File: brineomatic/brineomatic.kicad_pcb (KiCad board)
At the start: 2 copper layers, 117 parts, among them J1 SENSOR, J10 Solenoid, J11 Solenoid, J12 SENSOR, J13 SERVO, J14 TDS, J15 POWER, J2 Conn_01x03, J3 Conn_01x03, J4 THERMISTOR, J5 SERVO, J6 Solenoid, J7 MOTOR, J8 Solenoid, J9 Solenoid, Q1 AO3400A, Q2 AON7524, Q3 AO3400A, Q4 AO3400A, Q5 AO3400A, U1 ESP32-S3-DEVKITC, U2 XL1509-5.0, U3 ADS1115IDGS, U4 DRV8871DDA, U5 XL1509-5.0, U6 XL1509-5.0

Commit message: starting to look good.
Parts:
- removed C18: 100nF, Capacitor_SMD:C_0805_2012Metric_Pad1.18x1.45mm_HandSolder
- removed C19: 10uF/35v, Capacitor_SMD:C_1206_3216Metric_Pad1.33x1.80mm_HandSolder
- removed C20: 100uF / 10v, Capacitor_Tantalum_SMD:CP_EIA-3528-21_Kemet-B
- removed D10: LED, LED_SMD:LED_0805_2012Metric_Pad1.15x1.40mm_HandSolder
- removed D11: SS54, Diode_SMD:D_SMA
- removed D19: DSK24, Diode_SMD:D_SOD-123
- removed F4: mSMD150, Fuse:Fuse_1812_4532Metric_Pad1.30x3.40mm_HandSolder
- removed J13, J5: SERVO, Connector_PinHeader_2.54mm:PinHeader_1x03_P2.54mm_Vertical
- removed JP1, JP2: For Testing, Jumper:SolderJumper-2_P1.3mm_Open_RoundedPad1.0x1.5mm
- removed L4: SMMS0650-680M, Inductor_SMD:L_Chilisin_BMRB00060650
- removed Q2: AON7524, Package_DFN_QFN:DFN-8-1EP_3x3mm_P0.5mm_EP1.7x2.4mm
- removed R19, R20: 1k, Resistor_SMD:R_0805_2012Metric_Pad1.20x1.40mm_HandSolder
- removed R2, R32: 10.2K 0.1%, Resistor_SMD:R_1206_3216Metric_Pad1.30x1.75mm_HandSolder
- removed R21: 100k, Resistor_SMD:R_0805_2012Metric_Pad1.20x1.40mm_HandSolder
- removed R3, R33: 19.8K 0.1%, Resistor_SMD:R_1206_3216Metric_Pad1.30x1.75mm_HandSolder
- removed U6: XL1509-5.0, Package_SO:SOIC-8_3.9x4.9mm_P1.27mm
- C10: value 22uF / 63v -> 22uF / 50v; footprint Capacitor_SMD:CP_Elec_6.3x7.7 -> Capacitor_SMD:CP_Elec_6.3x5.4
- D3: value DSK24 -> DSK34
- J1, J12: value SENSOR -> PRESSURE; footprint TerminalBlock_Phoenix:TerminalBlock_Phoenix_PT-1,5-2-3.5-H_1x02_P3.50mm_Horizontal -> Connector_JST:JST_PH_S2B-PH-K_1x02_P2.00mm_Horizontal
- J10, J11, J6, J7, J9: footprint Connector_Phoenix_MSTB:PhoenixContact_MSTBA_2,5_2-G-5,08_1x02_P5.08mm_Horizontal -> Connector_Phoenix_MC:PhoenixContact_MC_1,5_2-G-3.5_1x02_P3.50mm_Horizontal
- J14: footprint TerminalBlock_Phoenix:TerminalBlock_Phoenix_PT-1,5-3-3.5-H_1x03_P3.50mm_Horizontal -> Connector_JST:JST_PH_S3B-PH-K_1x03_P2.00mm_Horizontal
- J15: footprint Connector_Phoenix_MSTB:PhoenixContact_MSTBA_2,5_2-G-5,08_1x02_P5.08mm_Horizontal -> Connector_Phoenix_MC_HighVoltage:PhoenixContact_MC_1,5_2-G-5.08_1x02_P5.08mm_Horizontal
- J2: value Conn_01x03 -> FLOWMETER; footprint TerminalBlock_Phoenix:TerminalBlock_Phoenix_PT-1,5-3-3.5-H_1x03_P3.50mm_Horizontal -> Connector_JST:JST_PH_S3B-PH-K_1x03_P2.00mm_Horizontal
- J3: value Conn_01x03 -> DS18B20; footprint TerminalBlock_Phoenix:TerminalBlock_Phoenix_PT-1,5-3-3.5-H_1x03_P3.50mm_Horizontal -> Connector_JST:JST_PH_S3B-PH-K_1x03_P2.00mm_Horizontal
- J4: footprint TerminalBlock_Phoenix:TerminalBlock_Phoenix_PT-1,5-2-3.5-H_1x02_P3.50mm_Horizontal -> Connector_JST:JST_PH_S2B-PH-K_1x02_P2.00mm_Horizontal
- J8: value Solenoid -> SERVOS; footprint Connector_Phoenix_MSTB:PhoenixContact_MSTBA_2,5_2-G-5,08_1x02_P5.08mm_Horizontal -> Connector_PinHeader_2.54mm:PinHeader_2x03_P2.54mm_Horizontal
- L1: value SMMS0650-680M -> 2.5A 68uH; footprint Inductor_SMD:L_Chilisin_BMRB00060650 -> Inductor_SMD:L_Sunlord_MWSA1003S
- R9: footprint Resistor_SMD:R_1206_3216Metric_Pad1.30x1.75mm_HandSolder -> Resistor_SMD:R_0805_2012Metric_Pad1.20x1.40mm_HandSolder
- U1: footprint yarrboard:Waveshare-ESP32-S3-dev-kit -> yarrboard:Waveshare-ESP32-S3-dev-kit-SMD
- moved H2 164.1 mm to (66.3, 89.2), turned to 180 degrees
- moved R10 161.5 mm to (69.2, 41.2)
- moved C3 161.3 mm to (69.2, 39.0)
- moved J4 157.6 mm to (65.5, 38.0), turned to -90 degrees
- moved R35 157.2 mm to (69.5, 57.5)
- moved R9 156.8 mm to (69.2, 36.8), turned to 180 degrees
- moved C21 152.2 mm to (69.5, 59.8), turned to 180 degrees
- moved J14 151.6 mm to (65.5, 55.0), turned to -90 degrees
- moved D20 148.1 mm to (69.5, 54.5)
- moved J1 140.7 mm to (65.5, 81.5), turned to -90 degrees
- moved J3 139.4 mm to (65.5, 45.5), turned to -90 degrees
- moved R8 138.0 mm to (68.5, 46.5), turned to 90 degrees
- moved D1 135.9 mm to (69.5, 84.2)
- moved C1 129.7 mm to (69.5, 79.5), turned to 180 degrees
- moved R4 129.6 mm to (69.5, 81.5)
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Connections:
- C1 pad 1: /ADC/ADC0 -> /ADC/ADC3
- C17 pad 1: /ADC/ADC1 -> /ADC/ADC2
- C21 pad 1: /ADC/ADC2 -> /ADC/ADC1
- C3 pad 1: /ADC/ADC3 -> /ADC/ADC0
- C6 pad 1: Net-(J5-Pin_2) -> Net-(U2-FB)
- F1 pad 1: Net-(J5-Pin_2) -> Net-(J8-Pin_3)
- J1 pad 2: Net-(J1-Pin_2) -> Net-(D1-COM)
- J12 pad 2: Net-(J12-Pin_2) -> Net-(D18-COM)
- J8 pad 1: +24V -> /Servo 1/SERVO1
- J8 pad 2: Net-(D11-A) -> /Servo 1/SERVO2
- R1 pad 2: Net-(J1-Pin_2) -> Net-(D1-COM)
- R10 pad 2: /ADC/ADC3 -> /ADC/ADC0
- R31 pad 2: Net-(J12-Pin_2) -> Net-(D18-COM)
- R34 pad 2: /ADC/ADC1 -> /ADC/ADC2
- R35 pad 2: /ADC/ADC2 -> /ADC/ADC1
- R4 pad 2: /ADC/ADC0 -> /ADC/ADC3
- U1 pad 17: unconnected-(U1-GPIO11-Pad17) -> /Flowmeter/OUTPUT
- U1 pad 27: unconnected-(U1-GPIO21-Pad27) -> /Solenoid Driver 1/INPUT
- U1 pad 28: unconnected-(U1-GPIO47-Pad28) -> /Solenoid Driver 2/INPUT
- U1 pad 29: unconnected-(U1-GPIO48-Pad29) -> /Solenoid Driver 3/INPUT
- U1 pad 33: unconnected-(U1-GPIO36-Pad33) -> /Solenoid Driver 4/INPUT
- U1 pad 36: unconnected-(U1-GPIO39-Pad36) -> /Servo 1/SERVO1
- U1 pad 37: unconnected-(U1-GPIO40-Pad37) -> /Servo 1/SERVO2
- U1 pad 38: unconnected-(U1-GPIO41-Pad38) -> /DC Motor Driver/IN1
- U1 pad 39: unconnected-(U1-GPIO42-Pad39) -> /DC Motor Driver/IN2
- U1 pad 6: unconnected-(U1-GPIO6-Pad6) -> /Temperature - DS18B20/OUTPUT
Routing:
- net +24V: track 0.00 -> 286.0 mm
- net +3.3V: track 0.00 -> 107.3 mm
- net +5V: track 0.00 -> 106.1 mm
- net ESP32_5V: track 0.00 -> 89.7 mm
- net /Solenoid Driver 4/INPUT: track 0.00 -> 42.1 mm
- net /ADC/ADC3: track 0.00 -> 39.7 mm, vias 0 -> 2
- net /Servo 1/SERVO2: track 0.00 -> 38.1 mm
- net Net-(U2-FB): track 0.00 -> 35.8 mm
- net /Servo 1/SERVO1: track 0.00 -> 35.5 mm
- net /ADC/ADC2: track 0.00 -> 31.2 mm, vias 0 -> 2
- net /Solenoid Driver 3/INPUT: track 0.00 -> 29.5 mm
- net SCL: track 0.00 -> 25.7 mm
- net Net-(D3-K): track 0.00 -> 20.6 mm
- net Net-(D8-K): track 0.00 -> 20.5 mm
- net /Solenoid Driver 2/INPUT: track 0.00 -> 20.3 mm
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- added copper zone on B.Cu, net GND
- added copper zone on F.Cu, net GND
- added copper zone on In1.Cu, net GND
- added copper zone on In2.Cu, net GND
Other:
- board outline added: 90 x 63.5 mm
- copper layers 2 -> 4
- board text added: "DC MOTOR + -"
- board text added: "S + -"
- board text added: "SERVOS"
- board text added: "SOLENOID 1"
- board text added: "SOLENOID 2"
- board text added: "SOLENOID 3"
- board text added: "SOLENOID 4"

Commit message: silkscreen and more layout tweaks.
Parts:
- added SYM1: Logo_Open_Hardware_Small, Symbol:OSHW-Logo_11.4x12mm_SilkScreen, F.Cu at (113.5, 61.2)
- added SYM2: Logo_Open_Hardware_Small, yarrboard:Logo Small, F.Cu at (91.5, 48.2)
- moved C9 1.08 mm to (117.4, 39.5), turned to 90 degrees
- moved C12 0.45 mm to (140.2, 50.7)
- moved C13 0.45 mm to (144.5, 50.7)
- moved C15 0.40 mm to (148.2, 51.3)
- moved D6 0.40 mm to (137.0, 41.9)
- moved C14 0.30 mm to (144.5, 52.7)
- moved R18 0.30 mm to (140.3, 52.7)
- moved D7 0.25 mm to (138.5, 47.5)
- moved C2 0.20 mm to (69.5, 69.3)
- moved L2 0.15 mm to (144.5, 47.1)
- moved J15 0.08 mm to (143.0, 33.1)
- moved J7 0.08 mm to (113.7, 33.1)
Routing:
- net +24V: track 286.0 -> 292.1 mm
- net /Flowmeter/OUTPUT: track 17.9 -> 19.1 mm
- net ESP32_5V: track 89.7 -> 90.4 mm
- net GND: vias 123 -> 139
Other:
- board text added: "-POWER+"
- board text added: "BRINEOMATIC"
- board text added: "FLOW LOPRES HIPRES"
- board text added: "REV A"
- board text added: "THERM DS18B20 TDS"
- board text added: "github.com/hoeken/brineomatic"

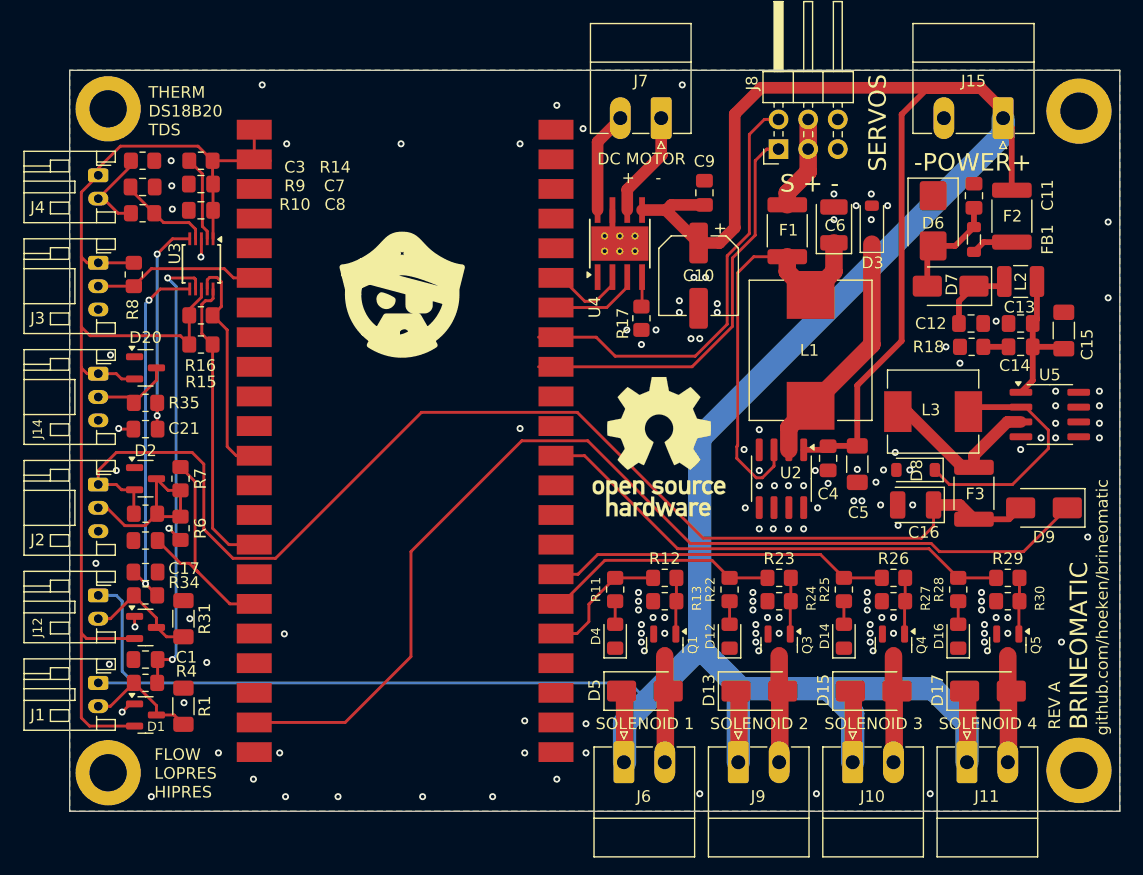
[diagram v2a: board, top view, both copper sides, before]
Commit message: updated bom and prepping for Rev A
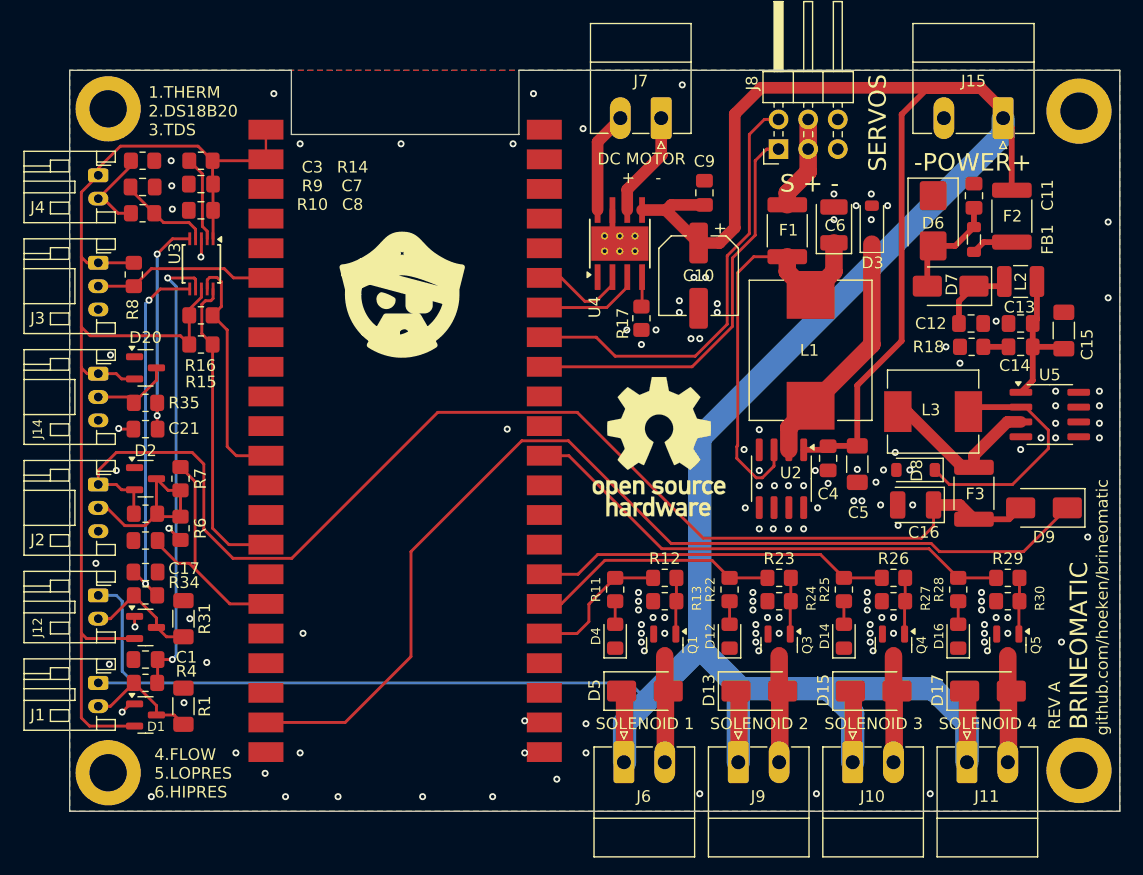
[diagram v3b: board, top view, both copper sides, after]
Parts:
- D7, D9: value SS34 -> SS54
- J1, J12: value PRESSURE -> ~
- J10, J11, J6, J9: value Solenoid -> 3.5MM
- J14: value TDS -> ~
- J15: value POWER -> 5.08MM
- J2: value FLOWMETER -> ~
- J3: value DS18B20 -> ~
- J4: value THERMISTOR -> ~
- J7: value MOTOR -> 3.5MM
- R14: value 10k -> 10K
- R17: value 30k -> 30K
- R7: value 5k -> 4.7K
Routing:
- net /Flowmeter/OUTPUT: track 19.1 -> 20.9 mm
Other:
- outline, holes or cut-outs redrawn
- board text added: "1.THERM 2.DS18B20 3.TDS"
- board text added: "4.FLOW 5.LOPRES 6.HIPRES"
- board text removed: "FLOW LOPRES HIPRES"
- board text removed: "THERM DS18B20 TDS"

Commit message: updates parts, footprints, etc.  ready for production.
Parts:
- J15: footprint Connector_Phoenix_MC_HighVoltage:PhoenixContact_MC_1,5_2-G-5.08_1x02_P5.08mm_Horizontal -> Connector_Phoenix_MSTB:PhoenixContact_MSTBA_2,5_2-G-5,08_1x02_P5.08mm_Horizontal
- R12, R23, R26, R29: value 1k -> 100R
- U3: value ADS1115IDGS -> ADS1115IDGSR
- moved J15 2.15 mm to (142.3, 35.1)
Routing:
- net Net-(U2-FB): track 35.8 -> 32.0 mm
- net +24V: track 292.1 -> 289.8 mm
- net /Servo 1/SERVO1: track 35.5 -> 36.6 mm
- net /Servo 1/SERVO2: track 38.1 -> 39.2 mm
- net GND: vias 139 -> 138
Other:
- board text added: "POWER - +"
- board text removed: "-POWER+"

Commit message: worked on schematic and layout a bit more.
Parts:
- removed C10: 22uF / 50v, Capacitor_SMD:CP_Elec_6.3x5.4
- removed the C9 at (117.4, 39.5)
- removed R17: 30K, Resistor_SMD:R_0805_2012Metric_Pad1.20x1.40mm_HandSolder
- added BZ1: Buzzer, yarrboard:Buzzer_FUET_9.6x9.6, F.Cu at (103.0, -2.00)
- added C18: 3.3nF, Capacitor_SMD:C_0603_1608Metric, F.Cu at (25.0, 48.3)
- added C2: 22uF 35v, Capacitor_SMD:CP_Elec_5x5.4, F.Cu at (159.0, 74.0)
- added D10: BAT54S, Package_TO_SOT_SMD:SOT-23, F.Cu at (31.9, 23.2)
- added D11: BAT54S, Package_TO_SOT_SMD:SOT-23, F.Cu at (20.1, 49.2)
- added F4: 20A, yarrboard:FUSE-TH_XF-508P-A-B, F.Cu at (145.5, 33.5)
- added J20: ~, Connector_JST:JST_PH_S3B-PH-K_1x03_P2.00mm_Horizontal, F.Cu at (67.0, 33.5)
- added Q2: AO3400A, Package_TO_SOT_SMD:SOT-23, F.Cu at (13.2, 39.5)
- added R2: 1k, Resistor_SMD:R_0603_1608Metric, F.Cu at (13.1, 43.2)
- added R20: 1k, Resistor_SMD:R_0603_1608Metric, F.Cu at (1.12, 33.9)
- added R3: 1k, Resistor_SMD:R_0603_1608Metric, F.Cu at (41.5, 22.3)
- added TP1: TestPoint, TestPoint:TestPoint_Pad_D1.5mm, F.Cu at (185.9, 71.3)
- added TP2: TestPoint, TestPoint:TestPoint_Pad_D1.5mm, F.Cu at (182.3, 67.8)
- added TP3: TestPoint, TestPoint:TestPoint_Pad_D1.5mm, F.Cu at (178.8, 71.3)
- added TP4: TestPoint, TestPoint:TestPoint_Pad_D1.5mm, F.Cu at (182.3, 71.3)
- added TP5: TestPoint, TestPoint:TestPoint_Pad_D1.5mm, F.Cu at (178.8, 67.8)
- added TP6: TestPoint, TestPoint:TestPoint_Pad_D1.5mm, F.Cu at (185.9, 67.8)
- C1, C11, C12, C13, C14, C17, C21, C3, C4, C7, C8: footprint Capacitor_SMD:C_0805_2012Metric_Pad1.18x1.45mm_HandSolder -> Capacitor_SMD:C_0603_1608Metric
- C9: renamed from C2; footprint Capacitor_SMD:C_0805_2012Metric_Pad1.18x1.45mm_HandSolder -> Capacitor_SMD:C_0603_1608Metric
- D12, D14, D16, D4: footprint LED_SMD:LED_0805_2012Metric_Pad1.15x1.40mm_HandSolder -> LED_SMD:LED_0603_1608Metric
- J4: footprint Connector_JST:JST_PH_S2B-PH-K_1x02_P2.00mm_Horizontal -> Connector_JST:JST_PH_S3B-PH-K_1x03_P2.00mm_Horizontal
- J7: value 3.5MM -> Conn_01x04; footprint Connector_Phoenix_MC:PhoenixContact_MC_1,5_2-G-3.5_1x02_P3.50mm_Horizontal -> Connector_JST:JST_PH_S4B-PH-K_1x04_P2.00mm_Horizontal
- R10: value 1k -> 2.2k; footprint Resistor_SMD:R_0805_2012Metric_Pad1.20x1.40mm_HandSolder -> Resistor_SMD:R_0603_1608Metric
- R11, R12, R13, R15, R16, R18, R22, R23, R24, R25, R26, R27, R28, R29, R30, R34, R35, R4, R5, R6, R7, R8: footprint Resistor_SMD:R_0805_2012Metric_Pad1.20x1.40mm_HandSolder -> Resistor_SMD:R_0603_1608Metric
- R14: value 10K -> 4.7K; footprint Resistor_SMD:R_0805_2012Metric_Pad1.20x1.40mm_HandSolder -> Resistor_SMD:R_0603_1608Metric
- R9: value 10K -> 1.2K; footprint Resistor_SMD:R_0805_2012Metric_Pad1.20x1.40mm_HandSolder -> Resistor_SMD:R_0603_1608Metric
- U4: value DRV8871DDA -> StepStick TMC2209; footprint Package_SO:Texas_HTSOP-8-1EP_3.9x4.9mm_P1.27mm_EP2.95x4.9mm_Mask2.4x3.1mm_ThermalVias -> yarrboard:StepStick TMC2209
- moved J7 66.2 mm to (149.0, 89.0), turned to 0 degrees
- moved R14 44.9 mm to (30.0, 44.5)
- moved U4 44.3 mm to (151.0, 61.0), turned to -90 degrees
- moved R9 39.3 mm to (30.0, 38.6), turned to 0 degrees
- moved R10 39.3 mm to (30.0, 41.5)
- moved C3 36.5 mm to (36.7, 22.4)
- moved SYM1 22.3 mm to (91.5, 65.0)
- moved R18 13.0 mm to (127.3, 52.7)
- moved C11 13.0 mm to (127.5, 39.8)
- moved C12 13.0 mm to (127.2, 50.7)
- moved C13 13.0 mm to (131.5, 50.7)
- moved C14 13.0 mm to (131.5, 52.7)
- moved C15 13.0 mm to (135.2, 51.3)
- moved C16 13.0 mm to (122.5, 66.2)
- moved C4 13.0 mm to (115.0, 62.2)
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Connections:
- C9 pad 1: /Flowmeter/OUTPUT -> /Product Flowmeter/OUTPUT
- D1 pad 3: Net-(D1-COM) -> /ADC/ADC3
- D18 pad 3: Net-(D18-COM) -> /ADC/ADC2
- D2 pad 2: +5V -> +3.3V
- D2 pad 3: Net-(D2-COM) -> /Product Flowmeter/OUTPUT
- D20 pad 3: Net-(D20-COM) -> /ADC/ADC1
- J1 pad 2: Net-(D1-COM) -> Net-(J1-Pin_2)
- J12 pad 2: Net-(D18-COM) -> Net-(J12-Pin_2)
- J14 pad 2: Net-(D20-COM) -> Net-(J14-Pin_2)
- J15 pad 1: +24V -> Net-(J15-Pin_1)
- J2 pad 2: Net-(D2-COM) -> Net-(J2-Pin_2)
- J8 pad 1: /Servo 1/SERVO1 -> /Servos/SERVO1
- J8 pad 2: /Servo 1/SERVO2 -> /Servos/SERVO2
- R1 pad 2: Net-(D1-COM) -> Net-(J1-Pin_2)
- R10 pad 1: Net-(J4-Pin_2) -> GND
- R10 pad 2: /ADC/ADC0 -> Net-(J20-Pin_2)
- R14 pad 1: Net-(U3-ALERT/RDY) -> Net-(J20-Pin_2)
- R14 pad 2: +3.3V -> /Brine Flowmeter/OUTPUT
- R31 pad 2: Net-(D18-COM) -> Net-(J12-Pin_2)
- R34 pad 1: Net-(D18-COM) -> Net-(J12-Pin_2)
- R35 pad 1: Net-(D20-COM) -> Net-(J14-Pin_2)
- R4 pad 1: Net-(D1-COM) -> Net-(J1-Pin_2)
- R5 pad 1: Net-(D2-COM) -> Net-(J2-Pin_2)
- R6 pad 2: Net-(D2-COM) -> Net-(J2-Pin_2)
- R7 pad 1: Net-(D2-COM) -> Net-(J2-Pin_2)
- R7 pad 2: /Flowmeter/OUTPUT -> /Product Flowmeter/OUTPUT
- R9 pad 1: GND -> Net-(J20-Pin_2)
- R9 pad 2: Net-(J4-Pin_2) -> +5V
- U1 pad 10: unconnected-(U1-GPIO17-Pad10) -> /Piezo/PIEZO
- U1 pad 11: unconnected-(U1-GPIO18-Pad11) -> ADC_ALERT/RDY
- U1 pad 17: /Flowmeter/OUTPUT -> /Product Flowmeter/OUTPUT
- U1 pad 18: unconnected-(U1-GPIO12-Pad18) -> /Brine Flowmeter/OUTPUT
- U1 pad 34: unconnected-(U1-GPIO37-Pad34) -> /Servos/SERVO1
- U1 pad 36: /Servo 1/SERVO1 -> /Servos/SERVO2
- U1 pad 37: /Servo 1/SERVO2 -> /Stepper Driver/TX
- U1 pad 38: /DC Motor Driver/IN1 -> /Stepper Driver/RX
- U1 pad 39: /DC Motor Driver/IN2 -> /Stepper Driver/EN
- U1 pad 40: unconnected-(U1-GPIO2-Pad40) -> /Stepper Driver/DIR
- U1 pad 41: unconnected-(U1-GPIO1-Pad41) -> /Stepper Driver/STEP
- U3 pad 2: Net-(U3-ALERT/RDY) -> ADC_ALERT/RDY
- U4 pad 1: GND -> /Stepper Driver/EN
- U4 pad 2: /DC Motor Driver/IN2 -> /Stepper Driver/MS1
- U4 pad 3: /DC Motor Driver/IN1 -> /Stepper Driver/MS2
- U4 pad 4: Net-(U4-ILIM) -> /Stepper Driver/RX
- U4 pad 5: +24V -> unconnected-(U4-PDN-Pad5)
- U4 pad 6: Net-(J7-Pin_1) -> unconnected-(U4-CLK-Pad6)
- U4 pad 7: GND -> /Stepper Driver/STEP
- U4 pad 8: Net-(J7-Pin_2) -> /Stepper Driver/DIR
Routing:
- net +24V: track 289.8 -> 0.00 mm
- net +3.3V: track 107.3 -> 0.00 mm
- net +5V: track 106.1 -> 0.00 mm
- net ESP32_5V: track 90.4 -> 0.00 mm
- net /Solenoid Driver 4/INPUT: track 42.1 -> 0.00 mm
- net /ADC/ADC3: track 39.7 -> 0.00 mm, vias 2 -> 0
- net /Servo 1/SERVO2: track 39.2 -> 0.00 mm
- net /Servo 1/SERVO1: track 36.6 -> 0.00 mm
- net Net-(U2-FB): track 32.0 -> 0.00 mm
- net /ADC/ADC2: track 31.2 -> 0.00 mm, vias 2 -> 0
- net /Solenoid Driver 3/INPUT: track 29.5 -> 0.00 mm
- net SCL: track 25.7 -> 0.00 mm
- net /Flowmeter/OUTPUT: track 20.9 -> 0.00 mm
- net Net-(D8-K): track 20.9 -> 0.00 mm
- net Net-(D3-K): track 20.6 -> 0.00 mm
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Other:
- board size 90 x 63.5 mm -> 102 x 63.5 mm
- board text removed: "DC MOTOR + -"

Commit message: lots of progress on Rev B
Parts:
- removed C4: 100nF, Capacitor_SMD:C_0603_1608Metric
- removed C5: 10uF/35v, Capacitor_SMD:C_1206_3216Metric_Pad1.33x1.80mm_HandSolder
- removed C6: 100uF / 10v, Capacitor_Tantalum_SMD:CP_EIA-3528-21_Kemet-B
- removed D3: DSK34, Diode_SMD:D_SOD-123
- removed F1: mSMD150, Fuse:Fuse_1812_4532Metric_Pad1.30x3.40mm_HandSolder
- removed L1: 2.5A 68uH, Inductor_SMD:L_Sunlord_MWSA1003S
- removed TP1, TP2, TP3, TP4, TP5, TP6: TestPoint, TestPoint:TestPoint_Pad_D1.5mm
- removed U2: XL1509-5.0, Package_SO:SOIC-8_3.9x4.9mm_P1.27mm
- added R17: 10k, Resistor_SMD:R_0603_1608Metric, F.Cu at (134.2, 62.5)
- added R19: 10k, Resistor_SMD:R_0603_1608Metric, F.Cu at (136.8, 62.5)
- J3: value ~ -> THERM
- moved R20 141.0 mm to (139.2, 62.5), turned to -90 degrees
- moved Q2 100.3 mm to (110.1, 65.7)
- moved R2 100.3 mm to (110.0, 69.3)
- moved BZ1 71.0 mm to (119.2, 67.1), turned to -90 degrees
- moved D11 61.0 mm to (75.4, 75.0), turned to 180 degrees
- moved C18 58.4 mm to (75.4, 77.8)
- moved J7 56.5 mm to (142.5, 33.0), turned to 180 degrees
- moved R10 55.4 mm to (71.9, 77.8), turned to 180 degrees
- moved R9 55.0 mm to (71.9, 74.2)
- moved R14 52.4 mm to (71.9, 76.0)
- moved D10 45.4 mm to (71.8, 44.8), turned to 90 degrees
- moved J20 42.2 mm to (67.0, 75.8)
- moved C3 40.5 mm to (72.8, 40.8), turned to 90 degrees
- moved R3 34.8 mm to (71.0, 40.8), turned to 90 degrees
- moved D9 32.0 mm to (108.9, 46.0), turned to -90 degrees
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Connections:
- J8 pad 3: Net-(J8-Pin_3) -> +5V
- J8 pad 4: Net-(J8-Pin_3) -> +5V
- Q2 pad 2: GNDD -> GND
- R20 pad 1: /Stepper Driver/TX -> TMC2209_RX
- U1 pad 11: ADC_ALERT/RDY -> unconnected-(U1-GPIO18-Pad11)
- U1 pad 17: /Product Flowmeter/OUTPUT -> /Brine Flowmeter/OUTPUT
- U1 pad 18: /Brine Flowmeter/OUTPUT -> /Product Flowmeter/OUTPUT
- U1 pad 37: /Stepper Driver/TX -> /Stepper Driver/RX
- U1 pad 38: /Stepper Driver/RX -> /Stepper Driver/DIAG
- U1 pad 7: unconnected-(U1-GPIO7-Pad7) -> ADC_ALERT/RDY
- U1 pad 8: unconnected-(U1-GPIO15-Pad8) -> TMC2209_RX
- U4 pad 17: Net-(U4-VREF) -> unconnected-(U4-VREF-Pad17)
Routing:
- net SCL: track 0.00 -> 26.2 mm
- net /Temperature - DS18B20/OUTPUT: track 0.00 -> 25.7 mm
- net /ADC/ADC3: track 0.00 -> 22.3 mm
- net SDA: track 0.00 -> 13.8 mm
- net /ADC/ADC2: track 0.00 -> 13.6 mm
- net ADC_ALERT/RDY: track 0.00 -> 10.1 mm
- net Net-(Q5-G): track 0.00 -> 7.92 mm
- net Net-(Q3-G): track 0.00 -> 7.92 mm
- net Net-(Q1-G): track 0.00 -> 7.92 mm
- net Net-(Q4-G): track 0.00 -> 7.92 mm
- net /ADC/ADC0: track 0.00 -> 3.93 mm
- net Net-(D15-A): track 0.00 -> 3.14 mm
- net Net-(D5-A): track 0.00 -> 3.14 mm
- net Net-(D13-A): track 0.00 -> 3.14 mm
- net Net-(D17-A): track 0.00 -> 3.14 mm
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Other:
- board size 102 x 63.5 mm -> 90 x 63.8 mm
- board text added: "BOOST PUMP"
- board text added: "BRINE FLOW"
- board text added: "BRINE TDS"
- board text added: "FAN"
- board text added: "FLUSH VALVE"
- board text added: "HI PRES"
- board text added: "HP PUMP"
- board text added: "LO PRES"
- board text added: "POWER GND | +24V"
- board text added: "PROD FLOW"
- board text added: "PROD TDS"
- board text added: "REV B"
- board text added: "STEPPER"
- board text added: "TEMP"
- board text removed: "1.THERM 2.DS18B20 3.TDS"
- board text removed: "4.FLOW 5.LOPRES 6.HIPRES"
- board text removed: "POWER - +"
- board text removed: "REV A"
- board text removed: "SOLENOID 1"
- board text removed: "SOLENOID 2"
- board text removed: "SOLENOID 3"
- board text removed: "SOLENOID 4"
